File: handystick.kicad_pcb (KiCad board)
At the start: 2 copper layers, 49.5 x 45 mm, 58 parts, among them CON1 AVR-ISP-6, CON2 USB-MINI-B, IC1 ATMEGA328P-A, P1 CONN_12, P2 CONN_12, SW1 SW_PUSH, SW2 SW_PUSH, X1 12MHz

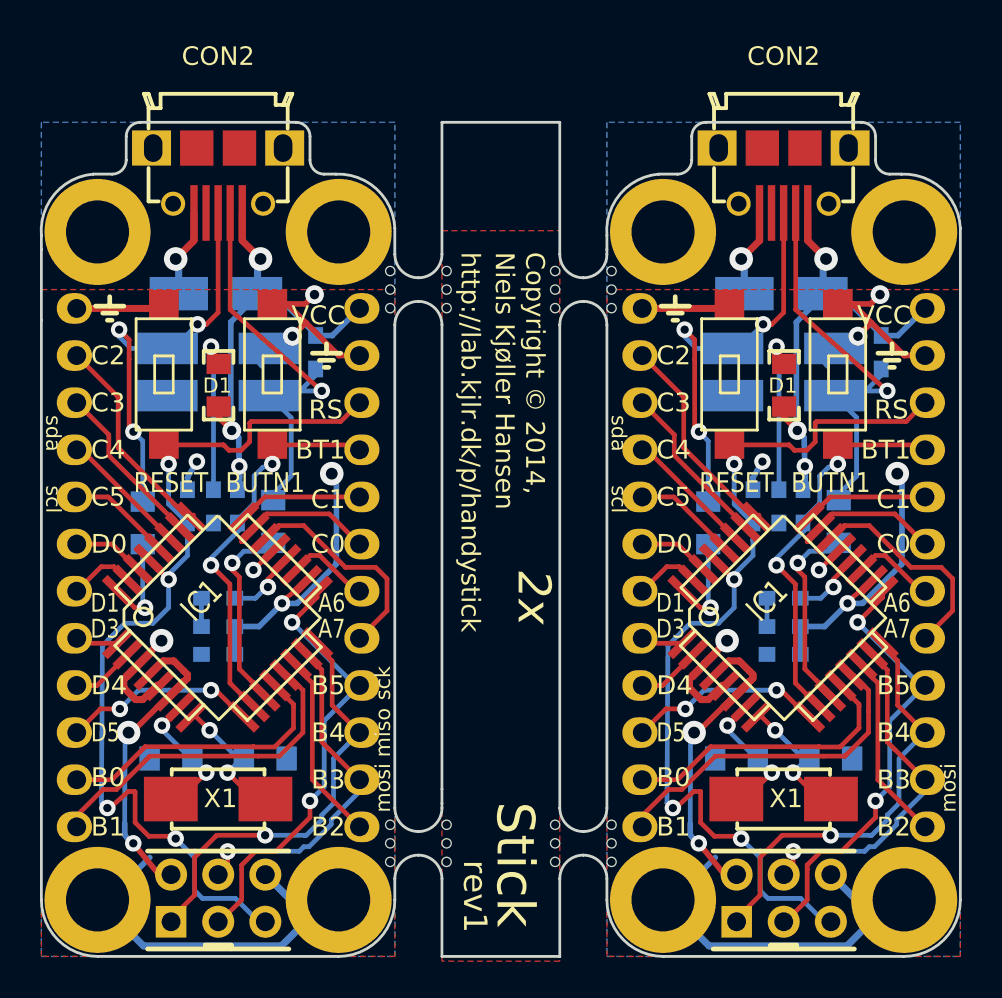
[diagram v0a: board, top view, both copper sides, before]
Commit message: cleaned up tree, added hex files for 328p and 88pa
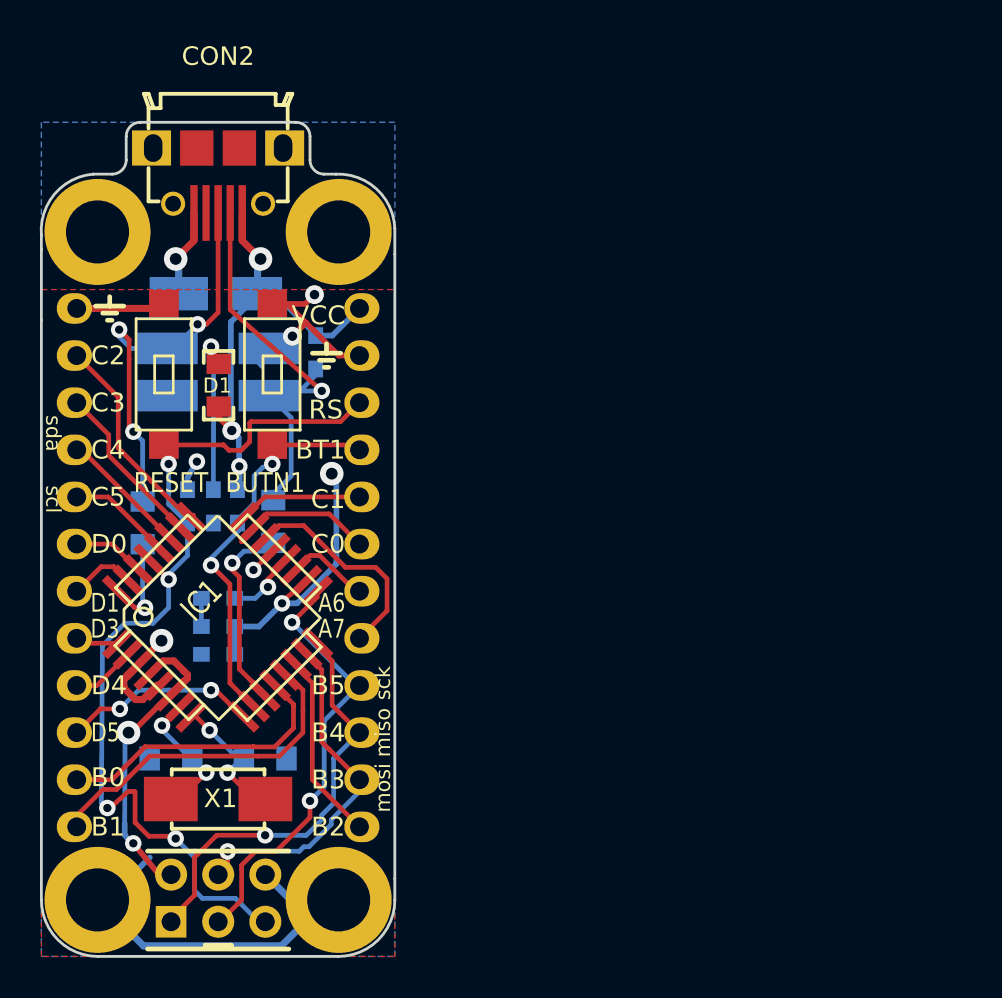
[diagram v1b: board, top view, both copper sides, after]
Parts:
- removed the 1PIN at (58.9, 72.3)
- removed the 1PIN at (71.9, 72.3)
- removed the 1PIN at (58.9, 36.3)
- removed the 1PIN at (71.9, 36.3)
- removed the C1 at (65.4, 59.0)
- removed the C2 at (65.4, 57.5)
- removed the C3 at (65.4, 56.0)
- removed the C4 at (62.9, 64.6)
- removed the C5 at (67.9, 64.6)
- removed the C6 at (65.4, 39.6)
- removed the CON1 at (65.4, 70.9)
- removed the CON2 at (65.4, 34.4)
- removed the D1 at (65.4, 44.5)
- removed the D2 at (65.4, 42.5)
- removed the D3 at (65.4, 45.1)
- removed the IC1 at (65.4, 57.0)
- removed Mousebites-3 (x4): VAL**, MySymbols:Mousebites-3
- removed the P1 at (57.8, 54.4)
- removed the P2 at (73.0, 54.4)
- removed the R1 at (63.8, 51.1)
- removed the R2 at (66.4, 51.1)
- removed the R3 at (65.2, 51.1)
- removed the R4 at (68.4, 51.9)
- removed the R5 at (61.3, 51.9)
- removed the R6 at (70.7, 42.7)
- removed the SW1 at (62.5, 43.9)
- removed the SW2 at (68.3, 43.9)
- removed the X1 at (65.4, 66.8)
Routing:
- net GND: track 124.5 -> 62.3 mm, vias 10 -> 5
- net VCC: track 116.0 -> 58.0 mm, vias 16 -> 8
- net /RESET: track 102.5 -> 51.2 mm, vias 8 -> 4
- net /SCK: track 49.3 -> 24.7 mm, vias 4 -> 2
- net Net-(CON2-Pad2): track 49.3 -> 24.7 mm, vias 2 -> 1
- net /MISO: track 46.4 -> 23.2 mm, vias 2 -> 1
- net Net-(CON2-Pad3): track 44.0 -> 22.0 mm, vias 6 -> 3
- net /PROG: track 43.6 -> 21.8 mm, vias 4 -> 2
- net /MOSI: track 38.0 -> 19.0 mm, vias 2 -> 1
- net /PB1: track 36.7 -> 18.3 mm
- net /PB0: track 31.4 -> 15.7 mm
- net /ADC7: track 23.9 -> 11.9 mm
- net /ADC2: track 23.1 -> 11.6 mm
- net /PD5: track 21.9 -> 10.9 mm, vias 4 -> 2
- net /USBD-: track 20.9 -> 10.4 mm, vias 2 -> 1
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- removed copper zone on F.Cu, net (none)
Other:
- board size 49.5 x 45 mm -> 19.1 x 45 mm
- board text removed: "2x"
- board text removed: "Copyright © 2014, Niels Kjøller Hansen"
- board text removed: "http://lab.kjlr.dk/p/handystick"
